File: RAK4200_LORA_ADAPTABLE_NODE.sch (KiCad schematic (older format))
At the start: 13 parts, among them J1 Screw_Terminal_01x03, J2 Screw_Terminal_01x03, J3 Conn_01x11_Male, J4 Conn_01x11_Male, U1 RAK4200

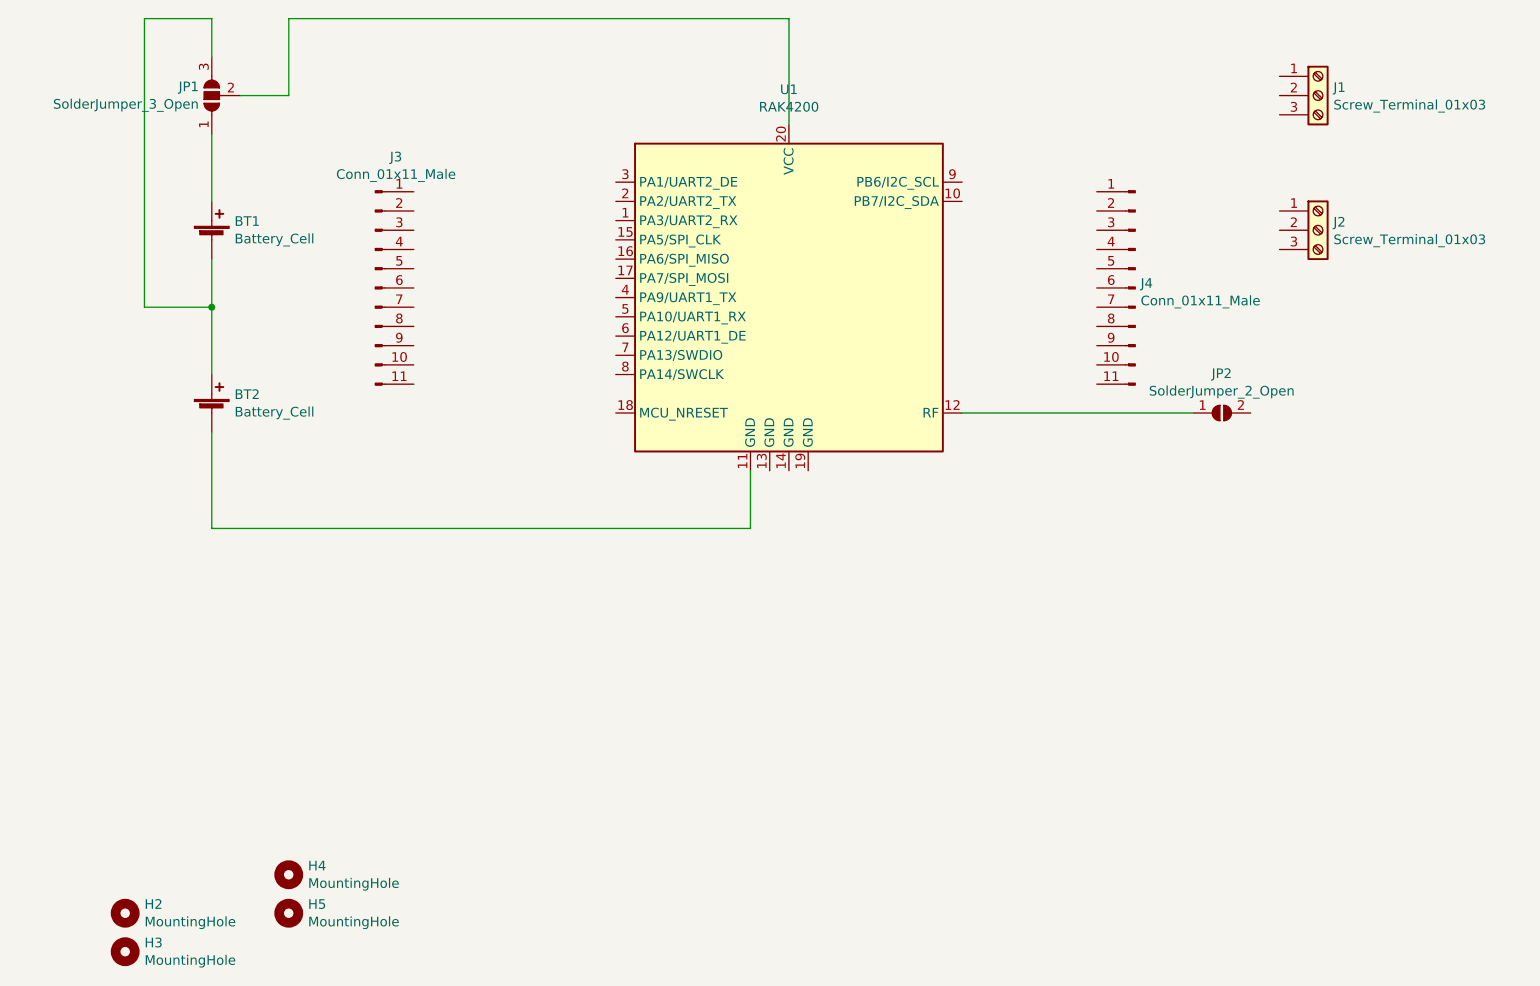
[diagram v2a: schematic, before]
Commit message: all I/O already connected
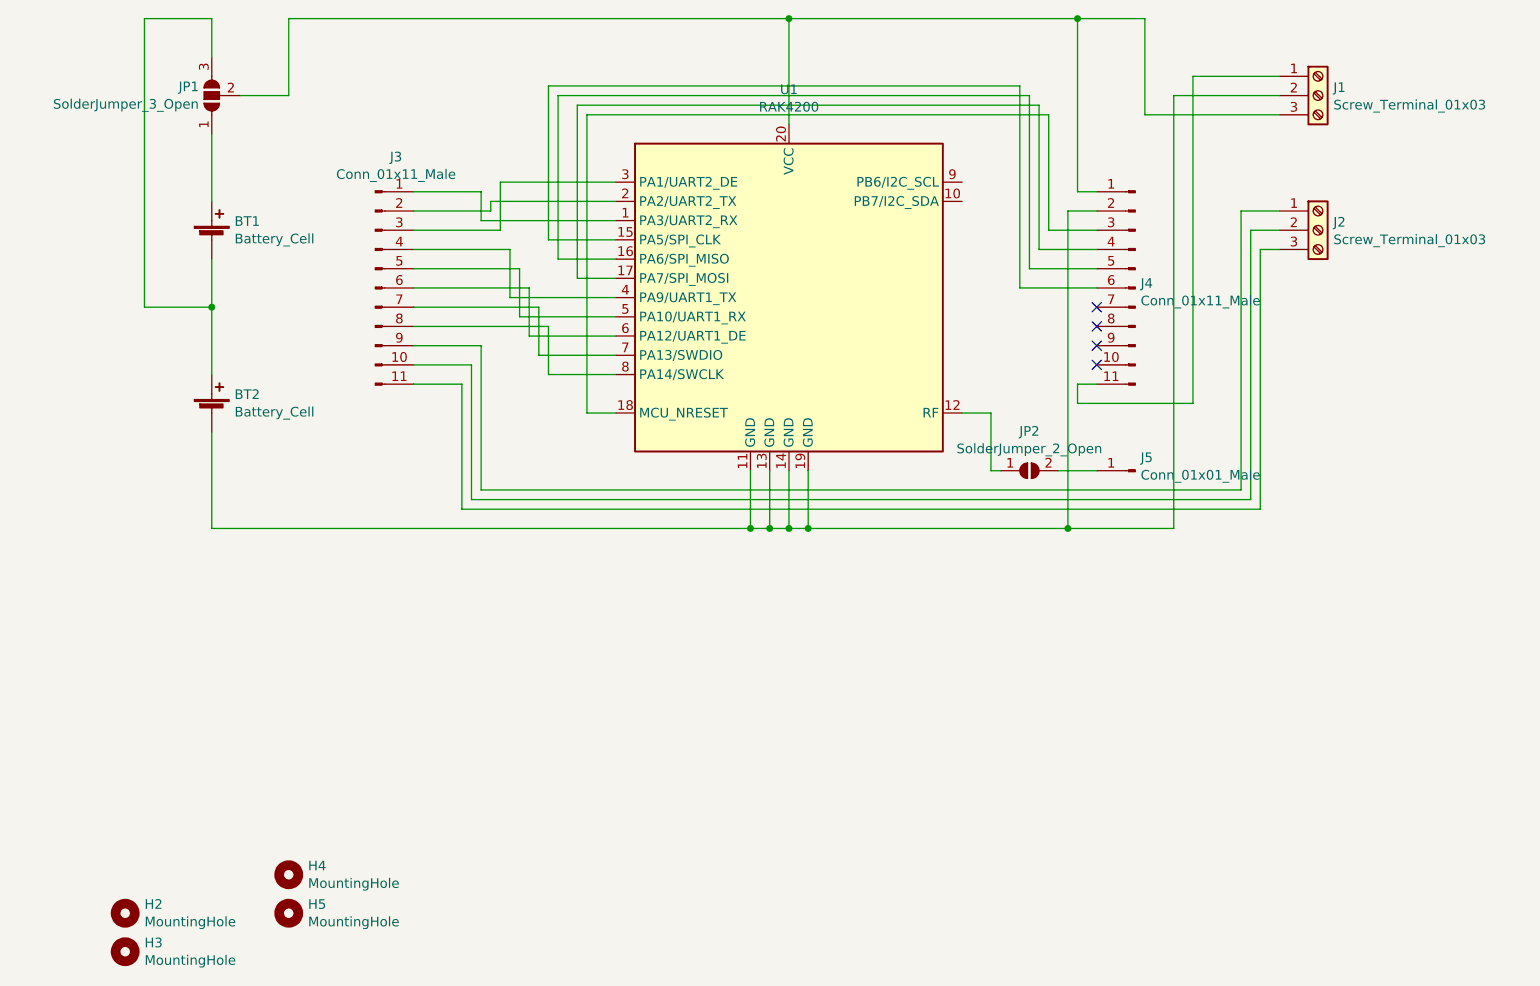
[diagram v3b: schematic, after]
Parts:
- added J5: Conn_01x01_Male, Connector_PinHeader_2.54mm:PinHeader_1x01_P2.54mm_Vertical, symbol Connector:Conn_01x01_Male
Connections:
- net at U1.1 (PA3/UART2_RX): now also J3.1 (Pin_1)
- net at BT2.2 (-), U1.11 (GND): now also J1.2 (Pin_2), J4.2 (Pin_2), U1.13 (GND), U1.14 (GND), U1.19 (GND)
- net at U1.15 (PA5/SPI_CLK): now also J4.6 (Pin_6)
- net at U1.16 (PA6/SPI_MISO): now also J4.5 (Pin_5)
- net at U1.17 (PA7/SPI_MOSI): now also J4.4 (Pin_4)
- net at U1.18 (MCU_NRESET): now also J4.3 (Pin_3)
- net at U1.2 (PA2/UART2_TX): now also J3.2 (Pin_2)
- net at JP1.2 (C), U1.20 (VCC): now also J1.3 (Pin_3), J4.1 (Pin_1)
- net at U1.3 (PA1/UART2_DE): now also J3.3 (Pin_3)
- net at U1.4 (PA9/UART1_TX): now also J3.4 (Pin_4)
- net at U1.5 (PA10/UART1_RX): now also J3.5 (Pin_5)
- net at U1.6 (PA12/UART1_DE): now also J3.6 (Pin_6)
- net at U1.7 (PA13/SWDIO): now also J3.7 (Pin_7)
- net at U1.8 (PA14/SWCLK): now also J3.8 (Pin_8)
- net at J1.1 (Pin_1): now also J4.11 (Pin_11)
- net at J2.1 (Pin_1): now also J3.9 (Pin_9)
- net at J2.2 (Pin_2): now also J3.10 (Pin_10)
- net at J2.3 (Pin_3): now also J3.11 (Pin_11)
- net at JP2.2 (B): now also J5.1 (Pin_1)
- no-connect marks 0 -> 4
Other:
- moved on the sheet: JP2
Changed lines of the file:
@@
 L Jumper:SolderJumper_2_Open JP2
 U 1 1 5F1A7BAB
-P 7900 4100
-F 0 "JP2" H 7900 4305 50  0000 C CNN
-F 1 "SolderJumper_2_Open" H 7900 4214 50  0000 C CNN
-F 2 "Jumper:SolderJumper-2_P1.3mm_Open_RoundedPad1.0x1.5mm" H 7900 4100 50  0001 C CNN
-F 3 "~" H 7900 4100 50  0001 C CNN
-	1    7900 4100
+P 6900 4400
+F 0 "JP2" H 6900 4605 50  0000 C CNN
+F 1 "SolderJumper_2_Open" H 6900 4514 50  0000 C CNN
+F 2 "Jumper:SolderJumper-2_P1.3mm_Open_RoundedPad1.0x1.5mm" H 6900 4400 50  0001 C CNN
+F 3 "~" H 6900 4400 50  0001 C CNN
+	1    6900 4400
 	1    0    0    -1
 $EndComp
@@
 Wire Wire Line
 	2650 3550 2650 3900
-Wire Wire Line
-	6550 4100 7750 4100
 $Comp
 L Connector:Conn_01x11_Male J3
@@
 	-1   0    0    -1
 $EndComp
+Wire Wire Line
+	5550 4400 5550 4700
+Wire Wire Line
+	5550 4700 5450 4700
+Connection ~ 5450 4700
+Wire Wire Line
+	5650 4400 5650 4700
+Wire Wire Line
+	5650 4700 5550 4700
+Connection ~ 5550 4700
+Wire Wire Line
+	5750 4400 5750 4700
+Wire Wire Line
+	5750 4700 5650 4700
+Connection ~ 5650 4700
+Wire Wire Line
+	8200 2450 7650 2450
+Wire Wire Line
+	7650 2450 7650 4700
+Wire Wire Line
+	7650 4700 7100 4700
+Connection ~ 5750 4700
+Wire Wire Line
+	8200 2550 7500 2550
+Wire Wire Line
+	7500 2550 7500 2050
+Wire Wire Line
+	7500 2050 7150 2050
+Connection ~ 5650 2050
+$Comp
+L Connector:Conn_01x01_Male J5
+U 1 1 5F1D34E0
+P 7450 4400
+F 0 "J5" H 7422 4332 50  0000 R CNN
+F 1 "Conn_01x01_Male" H 7422 4423 50  0000 R CNN
+F 2 "Connector_PinHeader_2.54mm:PinHeader_1x01_P2.54mm_Vertical" H 7450 4400 50  0001 C CNN
+F 3 "~" H 7450 4400 50  0001 C CNN
+	1    7450 4400
+	-1   0    0    1
+$EndComp
+Wire Wire Line
+	7050 4400 7250 4400
+Wire Wire Line
+	6750 4400 6700 4400
+Wire Wire Line
+	6700 4400 6700 4100
+Wire Wire Line
+	6700 4100 6550 4100
+Wire Wire Line
+	7250 2950 7150 2950
+Wire Wire Line
+	7150 2950 7150 2050
+Connection ~ 7150 2050
+Wire Wire Line
+	7150 2050 5650 2050
+Wire Wire Line
+	7250 3050 7100 3050
+Wire Wire Line
+	7100 3050 7100 4700
+Connection ~ 7100 4700
+Wire Wire Line
+	7100 4700 5750 4700
+Wire Wire Line
+	7250 3150 7000 3150
+Wire Wire Line
+	7000 3150 7000 2550
+Wire Wire Line
+	7000 2550 4600 2550
+Wire Wire Line
+	4600 2550 4600 4100
+Wire Wire Line
+	4600 4100 4750 4100
+Wire Wire Line
+	7250 3250 6950 3250
+Wire Wire Line
+	6950 3250 6950 2500
+Wire Wire Line
+	6950 2500 4550 2500
+Wire Wire Line
+	4550 2500 4550 3400
+Wire Wire Line
+	4550 3400 4750 3400
+Wire Wire Line
+	7250 3350 6900 3350
+Wire Wire Line
+	6900 3350 6900 2450
+Wire Wire Line
+	6900 2450 4450 2450
+Wire Wire Line
+	4450 2450 4450 3300
+Wire Wire Line
+	4450 3300 4750 3300
+Wire Wire Line
+	7250 3450 6850 3450
+Wire Wire Line
+	6850 3450 6850 2400
+Wire Wire Line
+	6850 2400 4400 2400
+Wire Wire Line
+	4400 2400 4400 3200
+Wire Wire Line
+	4400 3200 4750 3200
+Wire Wire Line
+	4750 3100 4050 3100
+Wire Wire Line
+	4050 3100 4050 2950
+Wire Wire Line
+	4050 2950 3700 2950
+Wire Wire Line
+	4750 3000 4100 3000
+Wire Wire Line
+	4100 3000 4100 3050
+Wire Wire Line
+	4100 3050 3700 3050
+Wire Wire Line
+	4750 2900 4150 2900
+Wire Wire Line
+	4150 2900 4150 3150
+Wire Wire Line
+	4150 3150 3700 3150
+Wire Wire Line
+	4750 3500 4200 3500
+Wire Wire Line
+	4200 3500 4200 3250
+Wire Wire Line
+	4200 3250 3700 3250
+Wire Wire Line
+	4750 3600 4250 3600
+Wire Wire Line
+	4250 3600 4250 3350
+Wire Wire Line
+	4250 3350 3700 3350
+Wire Wire Line
+	4750 3700 4300 3700
+Wire Wire Line
+	4300 3700 4300 3450
+Wire Wire Line
+	4300 3450 3700 3450
+Wire Wire Line
+	4750 3800 4350 3800
+Wire Wire Line
+	4350 3800 4350 3550
+Wire Wire Line
+	4350 3550 3700 3550
+Wire Wire Line
+	4750 3900 4400 3900
+Wire Wire Line
+	4400 3900 4400 3650
+Wire Wire Line
+	4400 3650 3700 3650
+Wire Wire Line
+	8200 2350 7750 2350
+Wire Wire Line
+	7750 2350 7750 4050
+Wire Wire Line
+	7750 4050 7150 4050
+Wire Wire Line
+	7150 4050 7150 3950
+Wire Wire Line
+	7150 3950 7250 3950
+Wire Wire Line
+	8200 3250 8100 3250
+Wire Wire Line
+	8100 3250 8100 4600
+Wire Wire Line
+	3950 4600 3950 3950
+Wire Wire Line
+	3950 3950 3700 3950
+Wire Wire Line
+	8100 4600 3950 4600
+Wire Wire Line
+	8200 3150 8050 3150
+Wire Wire Line
+	8050 3150 8050 4550
+Wire Wire Line
+	8050 4550 4000 4550
+Wire Wire Line
+	4000 4550 4000 3850
+Wire Wire Line
+	4000 3850 3700 3850
+Wire Wire Line
+	8200 3050 8000 3050
+Wire Wire Line
+	8000 3050 8000 4500
+Wire Wire Line
+	8000 4500 4050 4500
+Wire Wire Line
+	4050 4500 4050 3750
+Wire Wire Line
+	4050 3750 3700 3750
+NoConn ~ 7250 3550
+NoConn ~ 7250 3650
+NoConn ~ 7250 3750
+NoConn ~ 7250 3850
 $EndSCHEMATC
